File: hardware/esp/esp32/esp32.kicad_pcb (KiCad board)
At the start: 2 copper layers, 70.5 x 64 mm, 95 parts, among them U1 MCP23008-E/ML, U12 ESP32-WROOM-32E(4MB), U2 CH340C_C7464026, U3 SS8050_C2150, U4 MCP23008-E/ML, U5 MCP42010T-I/SL, U8 SS8050_C2150, U9 AMS1117-3_3

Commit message: wip
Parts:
- removed Center2: 5034801000, JLCPCB_footprint:FPC-SMD_5034801000
- added R4: 0805W8F4701T5E, JLCPCB_footprint:R0805, F.Cu at (152.2, 91.0)
- added TP11: TestPoint, TestPoint:TestPoint_Pad_D1.0mm, F.Cu at (146.5, 121.0)
- added TP37: TestPoint, TestPoint:TestPoint_Pad_D1.0mm, F.Cu at (148.5, 120.0)
- added TP38: TestPoint, TestPoint:TestPoint_Pad_D1.0mm, F.Cu at (152.0, 110.5)
- added TP39: TestPoint, TestPoint:TestPoint_Pad_D1.0mm, F.Cu at (147.5, 115.5)
- added U6: TS5A23157DGSR, JLCPCB_footprint:MSOP-10_L3.0-W3.0-P0.50-LS5.0-BL, F.Cu at (153.5, 117.5)
- added U7: IPFP051A30472R5, JLCPCB_footprint:FPC-SMD_4P-P0.50_C9900013912, F.Cu at (143.2, 118.7)
- R6: value 0805W8F4701T5E -> 0402WGF1002TCE; footprint JLCPCB_footprint:R0805 -> JLCPCB_footprint:R0402
- TP35, TP36: moved to B.Cu
- TP7, TP8: footprint TestPoint:TestPoint_Pad_1.5x1.5mm -> TestPoint:TestPoint_Pad_D1.0mm; moved to F.Cu
- moved TP3 58.5 mm to (183.0, 106.0)
- moved TP4 57.2 mm to (183.0, 113.5)
- moved TP1 57.1 mm to (183.0, 111.0)
- moved TP2 57.1 mm to (183.0, 108.5)
- moved U4 55.9 mm to (112.0, 128.5), turned to 90 degrees
- moved U5 45.1 mm to (161.0, 110.0), turned to -90 degrees
- moved D29 41.4 mm to (117.5, 130.0), turned to 90 degrees
- moved D28 40.0 mm to (119.5, 130.0), turned to 90 degrees
- moved D27 38.8 mm to (121.5, 130.0), turned to 90 degrees
- moved TP25 38.2 mm to (181.0, 123.0)
- moved D26 37.8 mm to (123.5, 130.0), turned to 90 degrees
- moved D25 37.2 mm to (125.5, 130.0), turned to 90 degrees
- moved D20 36.7 mm to (127.5, 130.0), turned to 90 degrees
- moved D1 36.6 mm to (129.5, 130.0), turned to 90 degrees
- moved TP11 33.9 mm to (179.0, 101.5)
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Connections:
- net /PSP Pins/Circle renamed circle
- net /PSP Pins/Cross renamed cross
- net /PSP Pins/Display renamed display
- net /PSP Pins/Down renamed down
- net /PSP Pins/Home renamed home
- net /PSP Pins/L1 renamed L1
- net /PSP Pins/Left renamed left
- net /PSP Pins/R1 renamed r1
- net /PSP Pins/Right renamed right
- net /PSP Pins/Sound renamed sound
- net /PSP Pins/Square renamed square
- net /PSP Pins/Triangle renamed triangle
- net /PSP Pins/Up renamed up
- net /PSP Pins/VolDown renamed voldown
- net /PSP Pins/VolUp renamed volup
- net /PSP Pins/power renamed power
- Analog1 pad 1: /PSP Pins/Y_1 -> /PSP Pins 2K/PSP_y
- Analog1 pad 10: /PSP Pins/Y_1 -> /PSP Pins 2K/Annalog_y
- Analog1 pad 2: /PSP Pins/X_1 -> /PSP Pins 2K/PSP_x
- Analog1 pad 8: /PSP Pins/X_1 -> /PSP Pins 2K/Analog_x
- Analog1 pad 9: /PSP Pins/+V -> /PSP Pins 2K/+V
- R5 pad 1: ESP_I2C_SDA -> ESP_I2C_SCL
- R6 pad 1: ESP_I2C_SCL -> unconnected-(R6-Pad1)
- R6 pad 2: +3.3V -> GND
- TP1 pad 1: /PSP Pins/X_1 -> unconnected-(TP1-Pad1)
- TP2 pad 1: /PSP Pins/Y_1 -> unconnected-(TP2-Pad1)
- TP3 pad 1: /PSP Pins/Y_1 -> unconnected-(TP3-Pad1)
- TP4 pad 1: /PSP Pins/X_1 -> unconnected-(TP4-Pad1)
- TP7 pad 1: Net-(U4-INT) -> Net-(U6-V+)
- TP8 pad 1: Net-(U1-INT) -> /PSP Pins 2K/+V
- U1 pad 7: Net-(U1-INT) -> unconnected-(U1-INT-Pad7)
- U12 pad 26: Net-(U12-IO4) -> Analog_toggle
- U4 pad 7: Net-(U4-INT) -> unconnected-(U4-INT-Pad7)
- U5 pad 6: /PSP Pins/Y_1 -> /PSP Pins 2K/digi-y
- U5 pad 7: /PSP Pins/+V -> /PSP Pins 2K/+V
- U5 pad 8: /PSP Pins/+V -> /PSP Pins 2K/+V
- U5 pad 9: /PSP Pins/X_1 -> /PSP Pins 2K/digi-X
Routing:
- net ESP_I2C_SDA: track 57.0 -> 116.8 mm, vias 4 -> 7
- net ESP_I2C_SCL: track 62.9 -> 121.5 mm, vias 5 -> 6
- net down: track 55.1 -> 4.24 mm, vias 6 -> 0
- net left: track 49.2 -> 2.83 mm, vias 2 -> 0
- net up: track 47.6 -> 3.45 mm, vias 2 -> 0
- net ESP_SPI_CS: track 59.4 -> 17.0 mm, vias 4 -> 0
- net /PSP Pins/Y_1: track 37.2 -> 0.00 mm, vias 4 -> 0
- net PSP_SELECT: track 19.5 -> 54.2 mm
- net PSP_START: track 36.6 -> 66.5 mm, vias 4 -> 2
- net /PSP Pins 2K/+V: track 0.00 -> 29.1 mm, vias 0 -> 2
- net /PSP Pins 2K/Analog_x: track 0.00 -> 26.7 mm, vias 0 -> 4
- net right: track 22.8 -> 47.3 mm
- net Net-(D20-A): track 27.7 -> 4.12 mm, vias 2 -> 0
- net /PSP Pins/X_1: track 23.3 -> 0.00 mm, vias 2 -> 0
- net Net-(D1-A): track 28.1 -> 5.26 mm, vias 2 -> 0
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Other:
- outline, holes or cut-outs redrawn
- board text removed: "dright"
- board text removed: "dup"
- board text removed: "home"
- board text removed: "l1"
- board text removed: "r1"
- board text removed: "square"

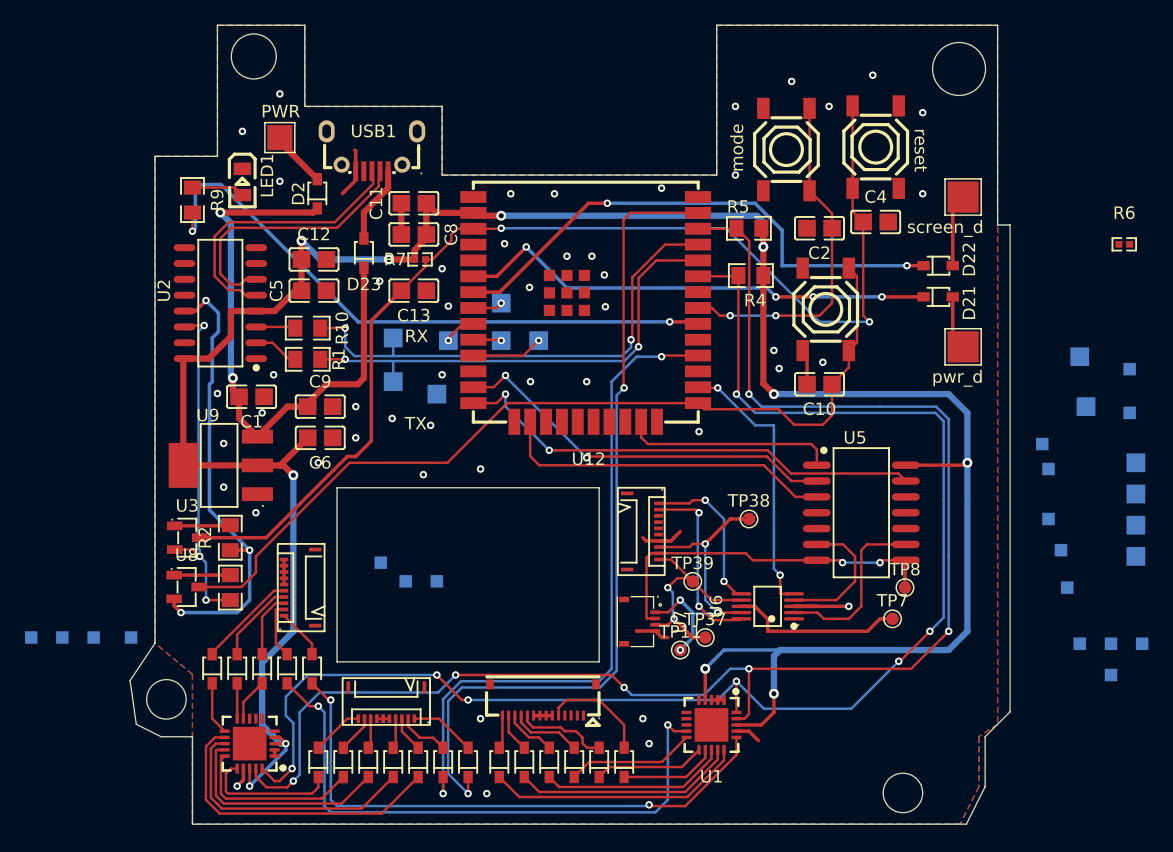
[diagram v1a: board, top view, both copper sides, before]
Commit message: Added hardware 0.2 - Added right FPC
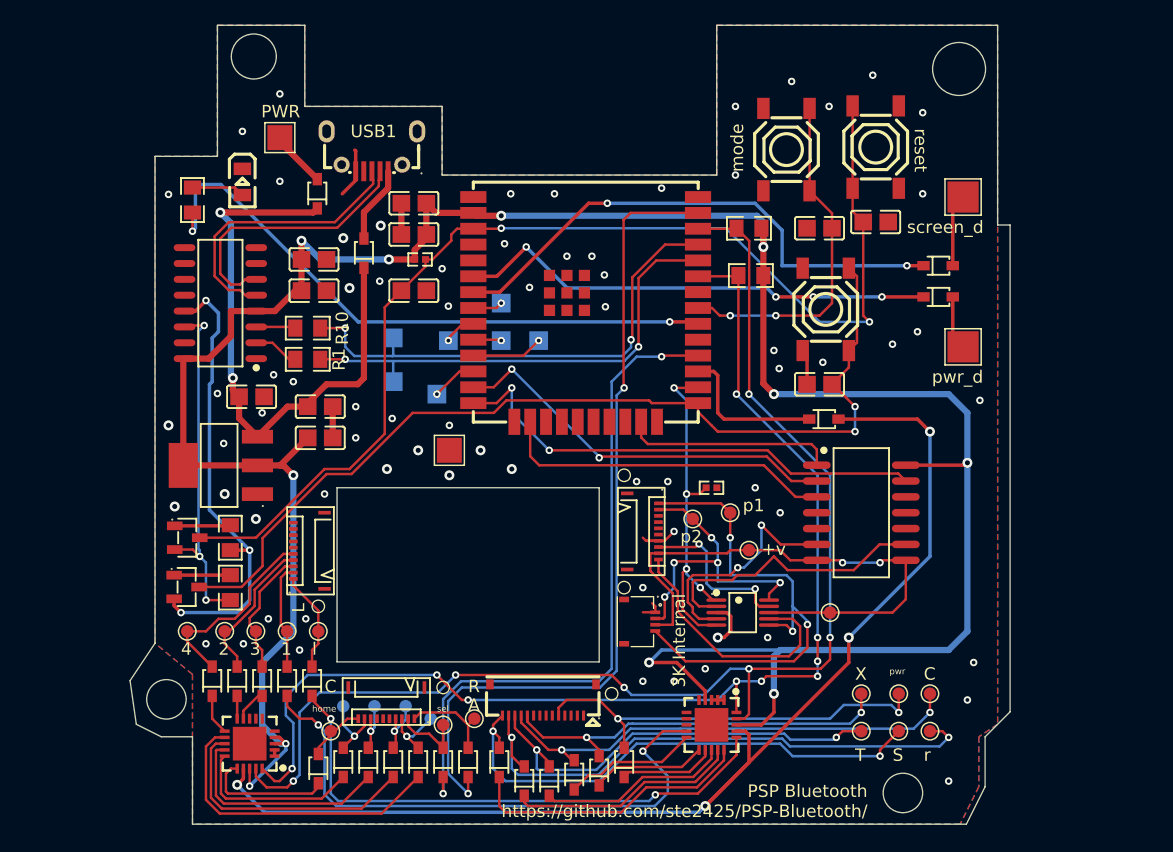
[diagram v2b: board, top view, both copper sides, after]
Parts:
- removed TP10, TP11: TestPoint, TestPoint:TestPoint_Pad_1.5x1.5mm
- removed TP11, TP37, TP38, TP39, TP8: TestPoint, TestPoint:TestPoint_Pad_D1.0mm
- added D13: 1N5819WS, JLCPCB_footprint:SOD-323_L1.8-W1.3-LS2.5-RD, F.Cu at (158.0, 102.5)
- TP1, TP2, TP3: footprint TestPoint:TestPoint_Pad_1.5x1.5mm -> TestPoint:TestPoint_Pad_D1.0mm; moved to F.Cu
- TP18, TP19, TP20, TP21, TP22, TP23, TP24, TP25, TP26, TP27, TP28, TP29, TP34, TP9: footprint TestPoint:TestPoint_Pad_1.0x1.0mm -> TestPoint:TestPoint_Pad_D1.0mm; moved to F.Cu
- TP30, TP31, TP32, TP33: footprint TestPoint:TestPoint_Pad_1.0x1.0mm -> TestPoint:TestPoint_Pad_D1.0mm
- TP4: footprint TestPoint:TestPoint_Pad_1.5x1.5mm -> TestPoint:TestPoint_Pad_2.0x2.0mm; moved to F.Cu
- moved TP33 67.2 mm to (119.5, 125.5)
- moved TP34 60.3 mm to (118.5, 127.5), turned to 0 degrees
- moved TP28 59.5 mm to (130.0, 126.5), turned to 0 degrees
- moved TP32 56.3 mm to (122.0, 125.5)
- moved TP4 55.7 mm to (128.0, 105.0), turned to 0 degrees
- moved TP31 53.6 mm to (124.5, 125.5)
- moved TP30 53.4 mm to (126.5, 126.5)
- moved TP29 53.0 mm to (127.5, 127.0), turned to 0 degrees
- moved TP24 41.3 mm to (166.5, 127.5), turned to 0 degrees
- moved TP26 41.3 mm to (164.0, 127.5), turned to 0 degrees
- moved R6 38.4 mm to (149.0, 108.0)
- moved TP2 35.6 mm to (147.5, 110.5), turned to 0 degrees
- moved TP1 32.5 mm to (150.5, 110.0), turned to 0 degrees
- moved TP3 31.8 mm to (152.0, 113.0), turned to 0 degrees
- moved TP25 20.5 mm to (161.0, 127.5), turned to 0 degrees
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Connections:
- Center1 pad 5: GND -> unconnected-(Center1-Pad5)
- Center1 pad 6: GND -> unconnected-(Center1-Pad6)
- Center1 pad 7: GND -> unconnected-(Center1-Pad7)
- Left1 pad 10: GND -> unconnected-(Left1-Pad10)
- Left1 pad 6: GND -> unconnected-(Left1-Pad6)
- Left1 pad 7: GND -> unconnected-(Left1-Pad7)
- Left1 pad 8: GND -> unconnected-(Left1-Pad8)
- Left1 pad 9: GND -> unconnected-(Left1-Pad9)
- R6 pad 1: unconnected-(R6-Pad1) -> Analog_toggle
- Right1 pad 6: GND -> unconnected-(Right1-Pad6)
- Right1 pad 7: GND -> unconnected-(Right1-Pad7)
- Right1 pad 8: GND -> unconnected-(Right1-Pad8)
- Right1 pad 9: GND -> unconnected-(Right1-Pad9)
- TP1 pad 1: unconnected-(TP1-Pad1) -> /PSP Pins 2K/PSP_y
- TP2 pad 1: unconnected-(TP2-Pad1) -> /PSP Pins 2K/PSP_x
- TP3 pad 1: unconnected-(TP3-Pad1) -> /PSP Pins 2K/+V
- TP4 pad 1: unconnected-(TP4-Pad1) -> GND
- TP7 pad 1: Net-(U6-V+) -> /PSP Pins 2K/+V
- U1 pad 17: GND -> Net-(D13-A)
- U12 pad 27: Net-(U12-IO16) -> GPIO_GND
- U4 pad 17: GND -> Net-(D13-A)
- U6 pad 8: Net-(U6-V+) -> /PSP Pins 2K/+V
- U7 pad 1: /PSP Pins 2K/Analog_x -> GND
- U7 pad 2: /PSP Pins 2K/+V -> /PSP Pins 2K/PSP_x
- U7 pad 3: /PSP Pins 2K/Annalog_y -> /PSP Pins 2K/+V
- U7 pad 4: GND -> /PSP Pins 2K/PSP_y
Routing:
- net Net-(D13-A): track 0.00 -> 93.6 mm, vias 0 -> 4
- net Net-(D8-A): track 3.10 -> 45.9 mm, vias 0 -> 2
- net Net-(D7-A): track 2.68 -> 42.1 mm, vias 0 -> 2
- net Net-(D10-A): track 5.65 -> 38.3 mm, vias 0 -> 2
- net Net-(D9-A): track 4.18 -> 34.4 mm, vias 0 -> 2
- net /PSP Pins 2K/PSP_y: track 12.8 -> 39.8 mm, vias 2 -> 3
- net Net-(D12-A): track 8.79 -> 33.5 mm, vias 0 -> 2
- net Net-(D11-A): track 7.37 -> 32.0 mm, vias 0 -> 2
- net ESP_I2C_SDA: track 116.8 -> 94.9 mm, vias 7 -> 9
- net ESP_I2C_SCL: track 121.5 -> 101.1 mm
- net /PSP Pins 2K/+V: track 29.1 -> 43.4 mm
- net Net-(U6-V+): track 13.9 -> 0.00 mm
- net /PSP Pins 2K/Analog_x: track 26.7 -> 13.2 mm, vias 4 -> 2
- net GPIO_GND: track 0.00 -> 12.2 mm
- net /PSP Pins 2K/PSP_x: track 14.8 -> 24.8 mm, vias 2 -> 5
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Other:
- board text added: "+v"
- board text added: "1"
- board text added: "2"
- board text added: "3"
- board text added: "3K"
- board text added: "3K Internal"
- board text added: "4"
- board text added: "A"
- board text added: "Analog"
- board text added: "C"
- board text added: "Center"
- board text added: "IO25"
- board text added: "IO26"
- board text added: "IO27"
- board text added: "IO32"
- board text added: "IO33"
- board text added: "L"
- board text added: "Left"
- board text added: "PSP Bluetooth v0.2 - Test Board Special thanks to: * abastos * benergylive * peterlustig1"
- board text added: "R"
- board text added: "Right"
- board text added: "S"
- board text added: "T"
- board text added: "X"
- board text added: "home"
- board text added: "l"
- board text added: "p1"
- board text added: "p2"
- board text added: "pwr"
- board text added: "r"
- board text added: "sel"
- board text added: "vol dwn"
- board text removed: "GPIO04"
- board text removed: "GPIO16"
- board text removed: "GPIO25"
- board text removed: "GPIO26"
- board text removed: "GPIO27"
- board text removed: "GPIO32"
- board text removed: "GPIO33"
- board text removed: "PSP Bluetooth v0.1 - Test Board Special thanks to: * abastos * benergylive * peterlustig1"
- board text removed: "Thanks for the support, motivation and just being cool!"
- board text removed: "circle"
- board text removed: "cross"
- board text removed: "ddown"
- board text removed: "dleft"
- board text removed: "power"
- board text removed: "select"
- board text removed: "start"
- board text removed: "triangle"
- board text removed: "vol down"
